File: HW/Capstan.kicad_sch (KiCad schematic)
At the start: 0 parts

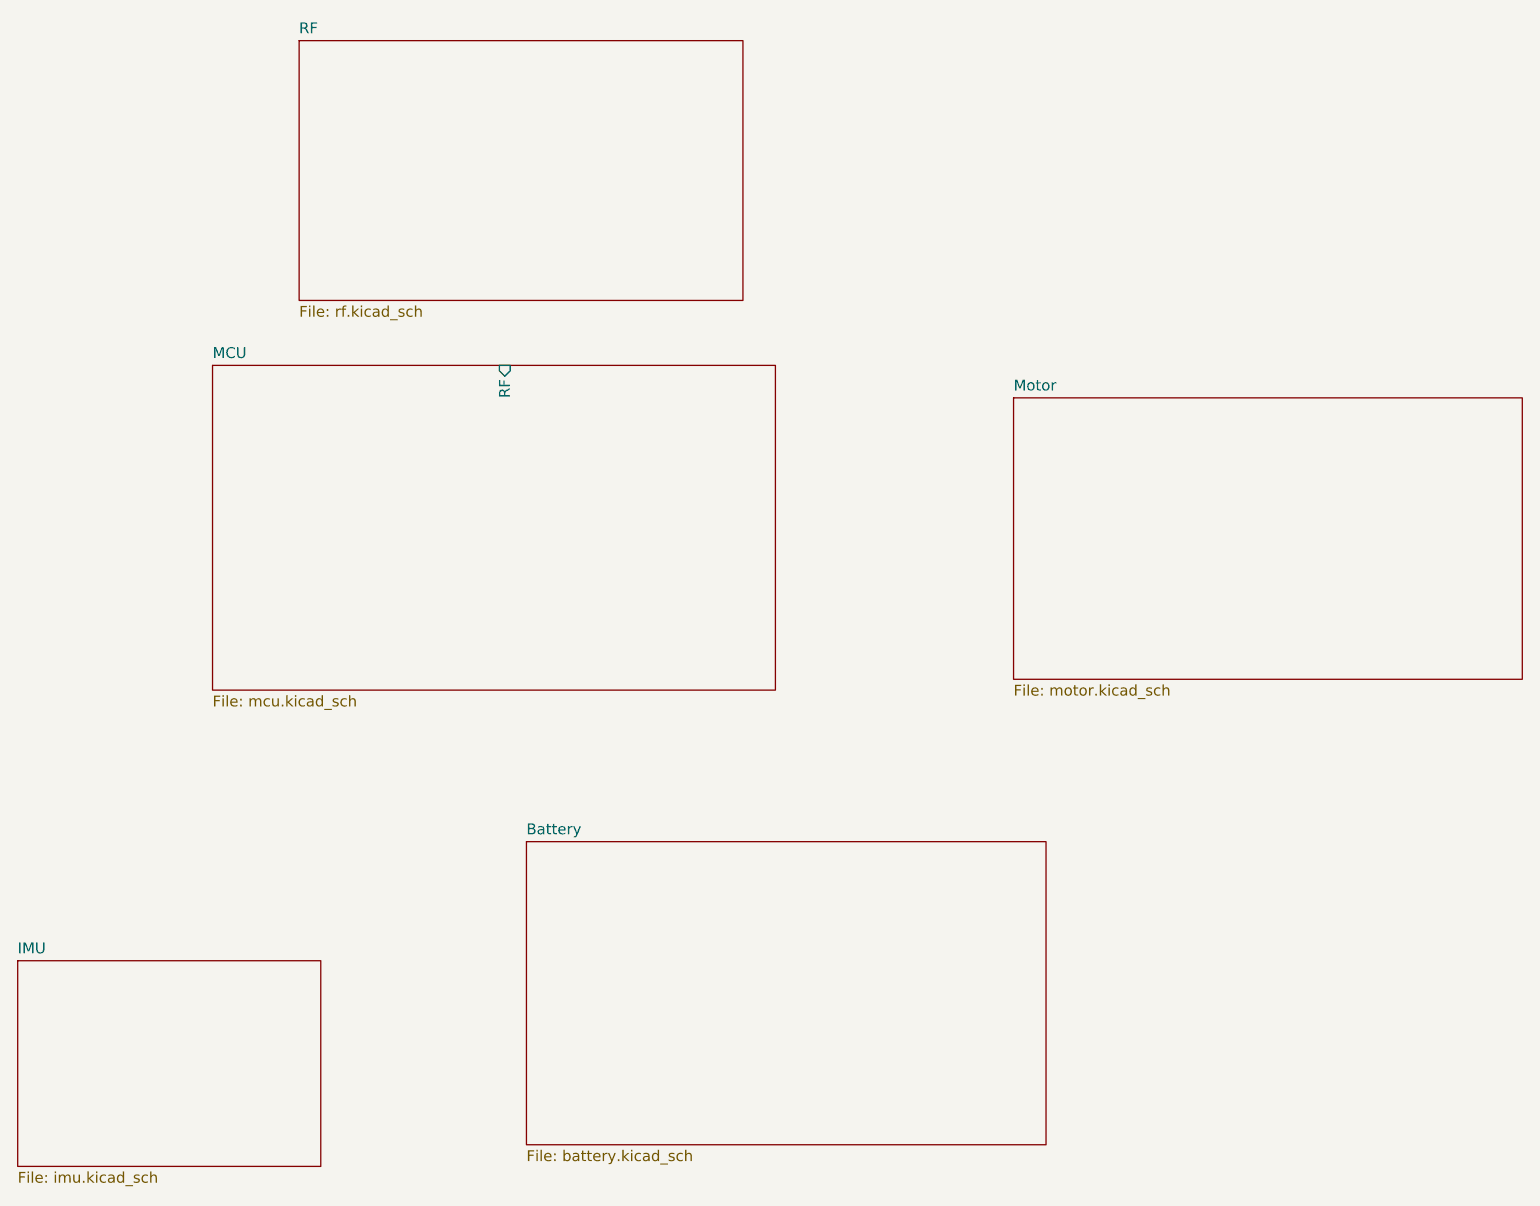
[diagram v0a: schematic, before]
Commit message: Almost first schematic draft (missing resistor values for STDRIVE current sensing and leds)
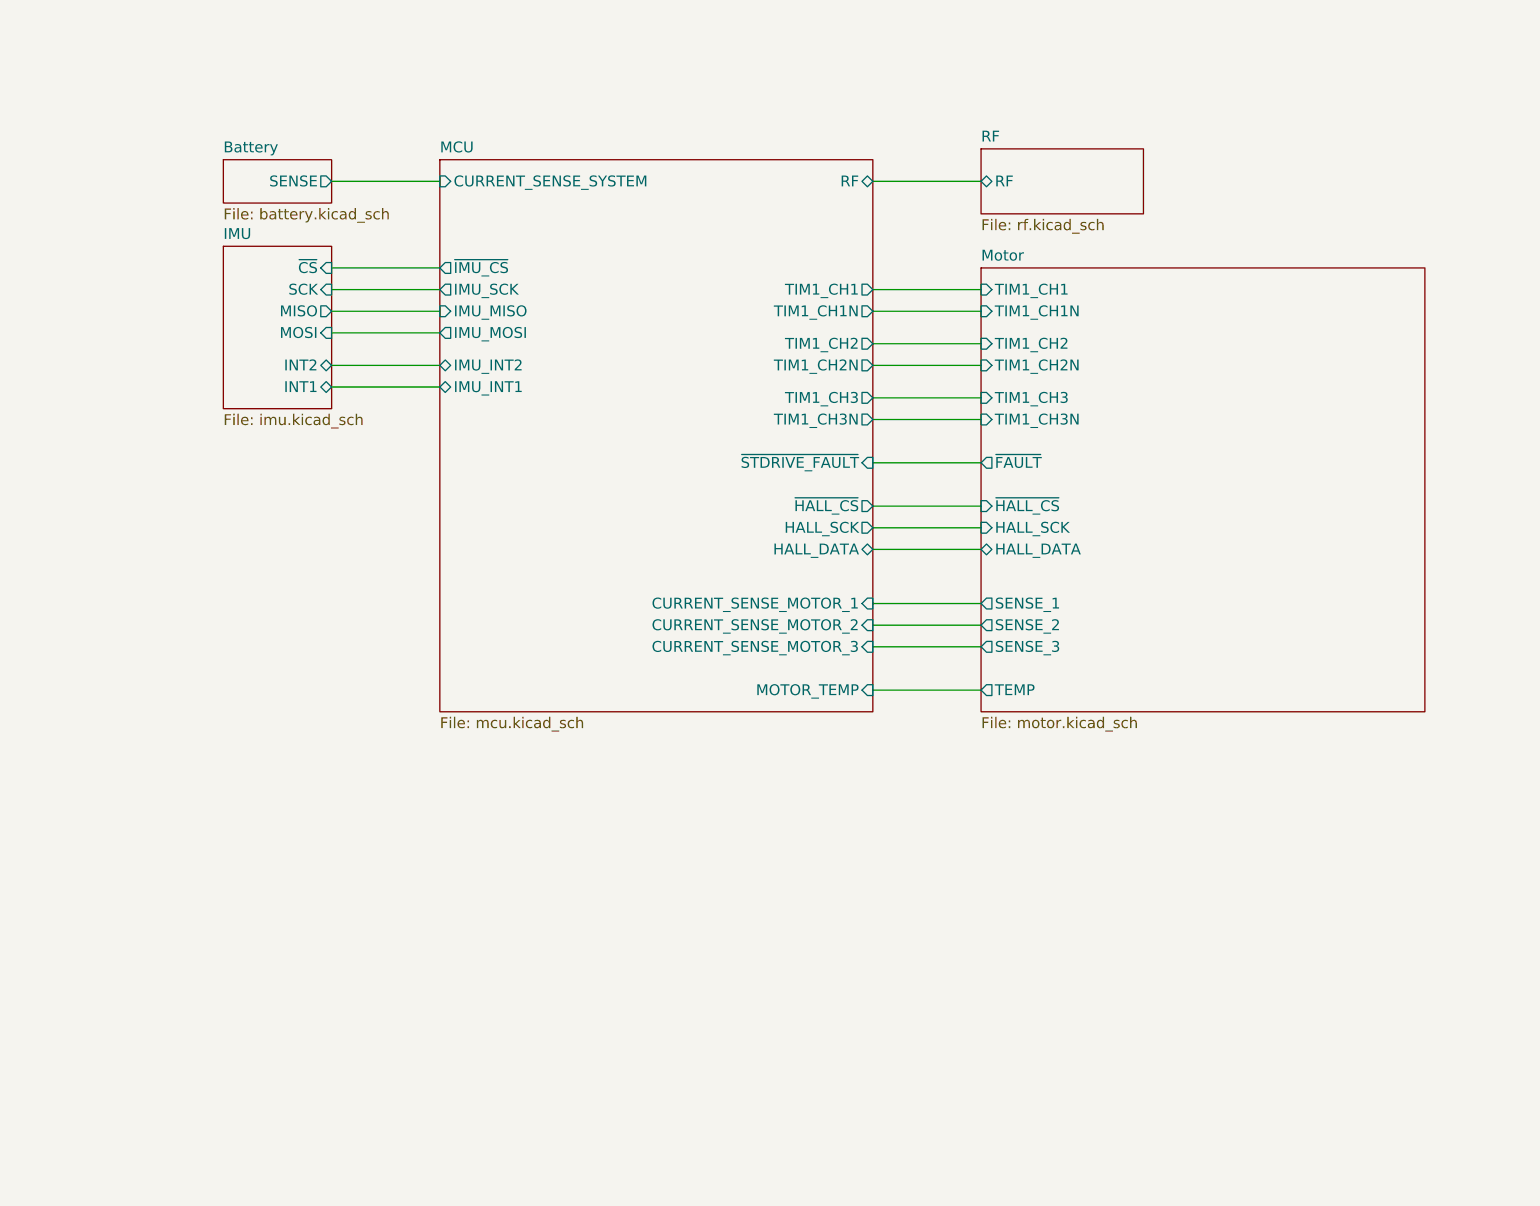
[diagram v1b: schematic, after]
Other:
- sheet Battery ports: added SENSE; removed none
- sheet IMU ports: added INT1, INT2, MISO, MOSI, SCK, ~{CS}; removed none
- sheet MCU ports: added CURRENT_SENSE_MOTOR_1, CURRENT_SENSE_MOTOR_2, CURRENT_SENSE_MOTOR_3, CURRENT_SENSE_SYSTEM, HALL_DATA, HALL_SCK, IMU_INT1, IMU_INT2, IMU_MISO, IMU_MOSI, IMU_SCK, MOTOR_TEMP, TIM1_CH1, TIM1_CH1N, TIM1_CH2, TIM1_CH2N, TIM1_CH3, TIM1_CH3N, ~{HALL_CS}, ~{IMU_CS}, ~{STDRIVE_FAULT}; removed none
- sheet Motor ports: added HALL_DATA, HALL_SCK, SENSE_1, SENSE_2, SENSE_3, TEMP, TIM1_CH1, TIM1_CH1N, TIM1_CH2, TIM1_CH2N, TIM1_CH3, TIM1_CH3N, ~{FAULT}, ~{HALL_CS}; removed none
- sheet RF ports: added RF; removed none

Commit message: Cleaned up and implemented some of Laimonas' feedback
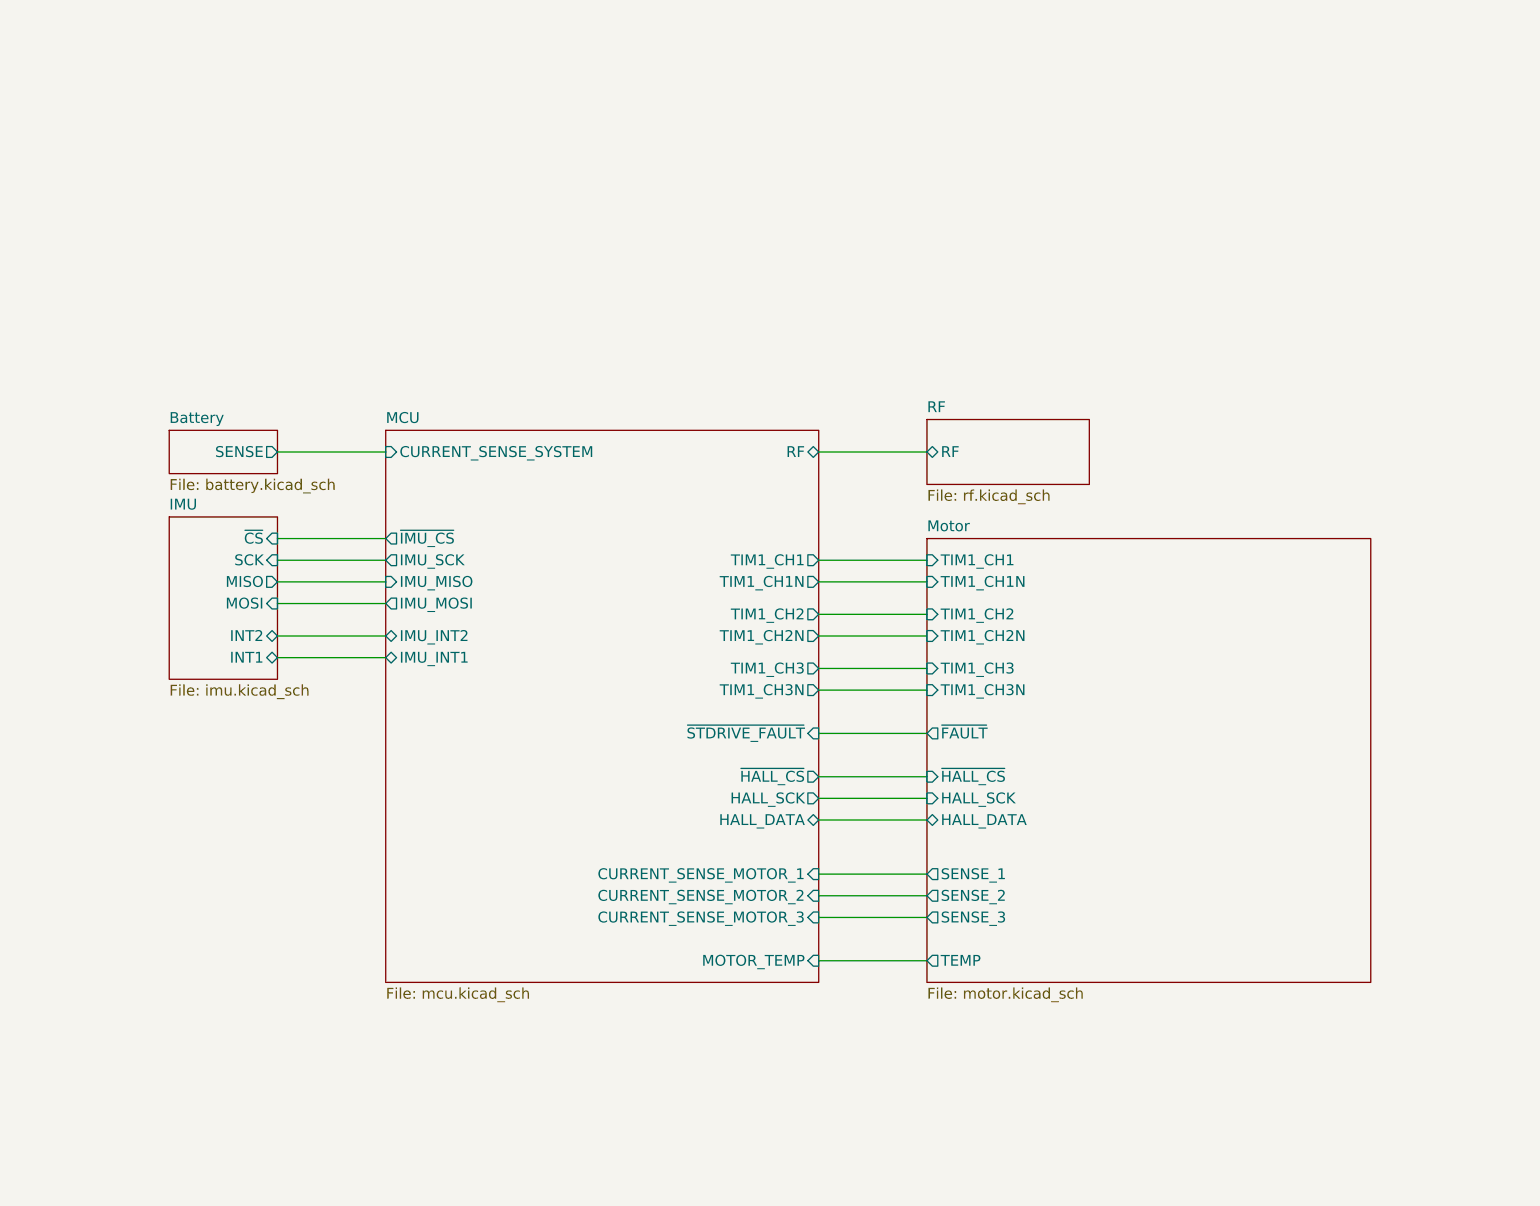
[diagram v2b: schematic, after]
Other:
- company: (none) -> Roberto Holmes
- title: (none) -> Capstan
